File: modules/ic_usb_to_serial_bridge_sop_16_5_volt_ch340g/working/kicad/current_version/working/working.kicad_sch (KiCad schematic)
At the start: 5 parts, among them U1 isp16ch340g

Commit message: gitignore update mainly and update
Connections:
- net rx_atmega328 is gone; now on net rx_ch340: 111.1
- net tx_atmega328 is gone; now on net tx_ch340: 11.1
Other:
- note added: "ch340328_tx_rx_patch_block"
- note removed: "atmega328_tx_rx_patch_block"

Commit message: a few module workings
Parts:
- added R1, R2: r6o102, oomlout_oomp_part_footprints:r6o102_electronic_resistor_0603_1000_ohm, symbol oomlout_oomp_part_symbols:r6o102_electronic_resistor_0603_1000_ohm
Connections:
- net rx_ch340: now also R2.2; no longer U1.3 (RXD)
- net tx_ch340: now also R1.2; no longer U1.2 (TXD)
- new net: R2.1, U1.3 (RXD)
- new net: R1.1, U1.2 (TXD)
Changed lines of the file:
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@@
   (junction (at 134.62 107.95) (diameter 0) (color 0 0 0 0)
   )
+  (bus_entry (at 133.35 101.6) (size 2.54 2.54)
+    (stroke (width 0) (type default))
+  )
   (wire (pts (xy 123.19 114.3) (xy 134.62 114.3))
     (stroke (width 0) (type default))
@@
     (stroke (width 0) (type default))
   )
+  (wire (pts (xy 157.48 76.2) (xy 157.48 73.66))
+    (stroke (width 0) (type default))
+  )
   (wire (pts (xy 121.92 96.52) (xy 124.46 96.52))
     (stroke (width 0) (type default))
   )
+  (wire (pts (xy 154.94 76.2) (xy 157.48 76.2))
+    (stroke (width 0) (type default))
+  )
   (wire (pts (xy 134.62 114.3) (xy 134.62 116.84))
     (stroke (width 0) (type default))
@@
     (stroke (width 0) (type default))
   )
+  (wire (pts (xy 160.02 78.74) (xy 160.02 73.66))
+    (stroke (width 0) (type default))
+  )
   (wire (pts (xy 144.78 78.74) (xy 147.32 78.74))
     (stroke (width 0) (type default))
@@
   )
   (wire (pts (xy 125.73 140.97) (xy 129.54 140.97))
+    (stroke (width 0) (type default))
+  )
+  (wire (pts (xy 154.94 78.74) (xy 160.02 78.74))
     (stroke (width 0) (type default))
   )
@@
     (effects (font (size 1.27 1.27)) (justify right bottom))
   )
-  (label "rx_ch340" (at 147.32 78.74 0) (fields_autoplaced)
+  (label "rx_ch340" (at 160.02 73.66 90) (fields_autoplaced)
     (effects (font (size 1.27 1.27)) (justify left bottom))
   )
@@
     (effects (font (size 1.27 1.27)) (justify right bottom))
   )
-  (label "tx_ch340" (at 147.32 76.2 0) (fields_autoplaced)
+  (label "tx_ch340" (at 157.48 73.66 90) (fields_autoplaced)
     (effects (font (size 1.27 1.27)) (justify left bottom))
   )
@@
         (path "/c9993764-076f-44f6-bf4c-6b69ce17c9e4"
           (reference "11") (unit 1)
+        )
+      )
+    )
+  )
+  (symbol (lib_id "oomlout_oomp_part_symbols:r6o102_electronic_resistor_0603_1000_ohm") (at 151.13 78.74 90) (unit 1)
+    (in_bom yes) (on_board yes) (dnp no)
+    (property "Reference" "R2" (at 151.13 78.74 90)
+      (effects (font (size 1.27 1.27)))
+    )
+    (property "Value" "r6o102" (at 151.13 81.28 90)
+      (effects (font (size 1.27 1.27)) hide)
+    )
+    (property "Footprint" "oomlout_oomp_part_footprints:r6o102_electronic_resistor_0603_1000_ohm" (at 151.13 80.518 90)
+      (effects (font (size 1.27 1.27)) hide)
+    )
+    (property "Datasheet" "https://github.com/oomlout/oomlout_oomp_v3/parts/electronic_resistor_0603_1000_ohm/datasheet.pdf" (at 151.13 78.74 0)
+      (effects (font (size 1.27 1.27)) hide)
+    )
+    (pin "1")
+    (pin "2")
+    (instances
+      (project "working"
+        (path "/12ef09fc-ac25-49d7-9ff1-a1bc8f30d19c"
+          (reference "R2") (unit 1)
         )
       )
@@
         )
       )
+    )
+  )
+  (symbol (lib_id "oomlout_oomp_part_symbols:r6o102_electronic_resistor_0603_1000_ohm") (at 151.13 76.2 90) (unit 1)
+    (in_bom yes) (on_board yes) (dnp no)
+    (property "Reference" "R1" (at 151.13 76.2 90)
+      (effects (font (size 1.27 1.27)))
+    )
+    (property "Value" "r6o102" (at 151.13 73.66 90)
+      (effects (font (size 1.27 1.27)))
+    )
+    (property "Footprint" "oomlout_oomp_part_footprints:r6o102_electronic_resistor_0603_1000_ohm" (at 151.13 77.978 90)
+      (effects (font (size 1.27 1.27)) hide)
+    )
+    (property "Datasheet" "https://github.com/oomlout/oomlout_oomp_v3/parts/electronic_resistor_0603_1000_ohm/datasheet.pdf" (at 151.13 76.2 0)
+      (effects (font (size 1.27 1.27)) hide)
+    )
+    (pin "1")
+    (pin "2")
+    (instances
+      (project "working"
+        (path "/12ef09fc-ac25-49d7-9ff1-a1bc8f30d19c"
+          (reference "R1") (unit 1)
+        )
+      )

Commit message: a few module fixes
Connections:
- net xtal_1 renamed xtal1
- net xtal_2 renamed xtal2
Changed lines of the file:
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@@
     (effects (font (size 1.27 1.27)) (justify left bottom))
   )
-  (label "xtal_2" (at 121.92 96.52 180) (fields_autoplaced)
+  (label "xtal2" (at 121.92 96.52 180) (fields_autoplaced)
     (effects (font (size 1.27 1.27)) (justify right bottom))
   )
-  (label "xtal_1" (at 121.92 91.44 180) (fields_autoplaced)
+  (label "xtal1" (at 121.92 91.44 180) (fields_autoplaced)
     (effects (font (size 1.27 1.27)) (justify right bottom))
   )

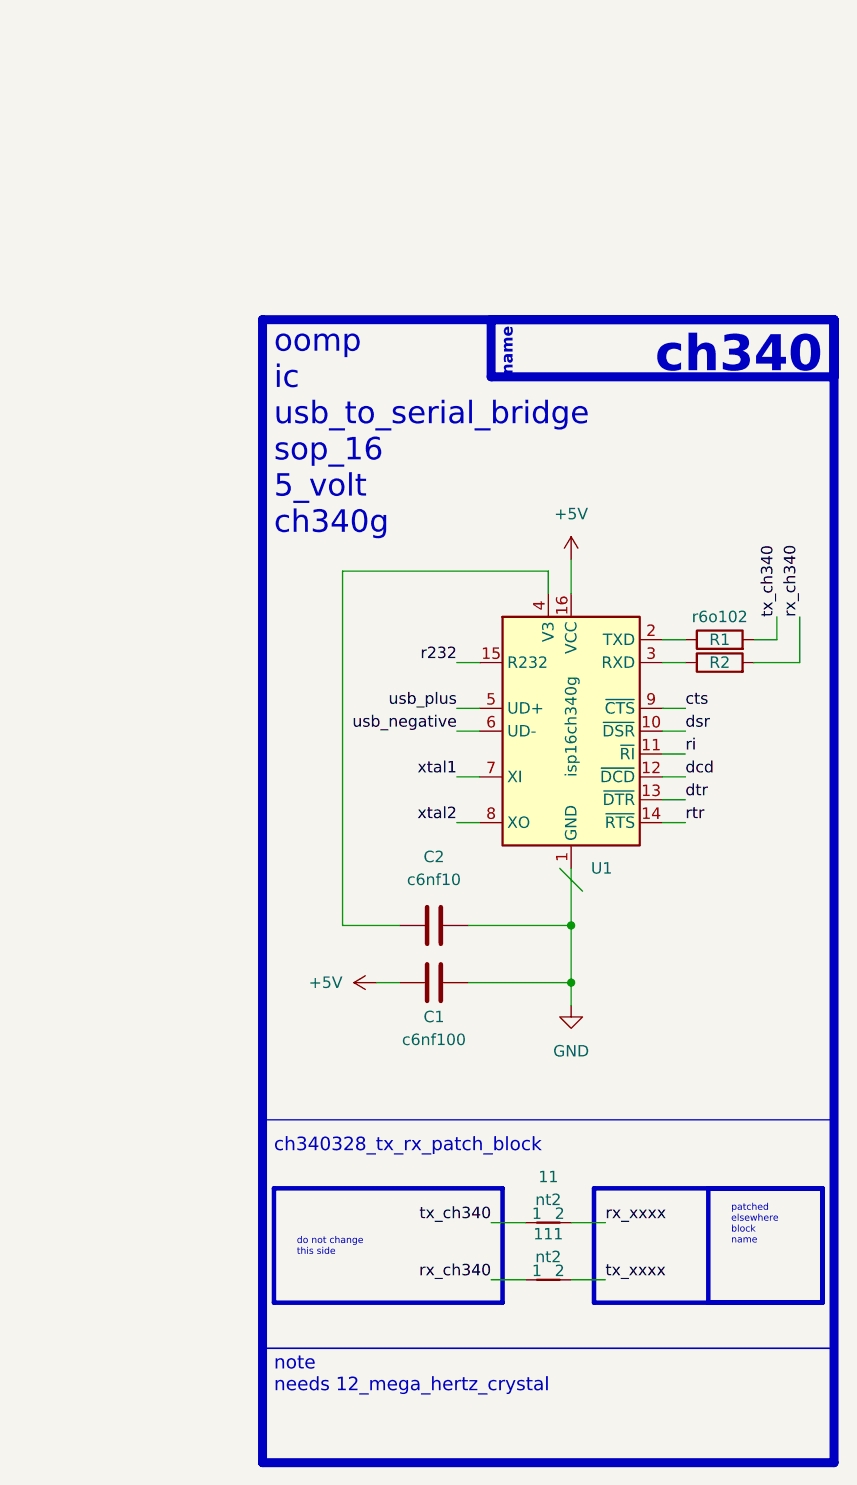
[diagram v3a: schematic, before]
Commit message: fixed formatting to be more consistent
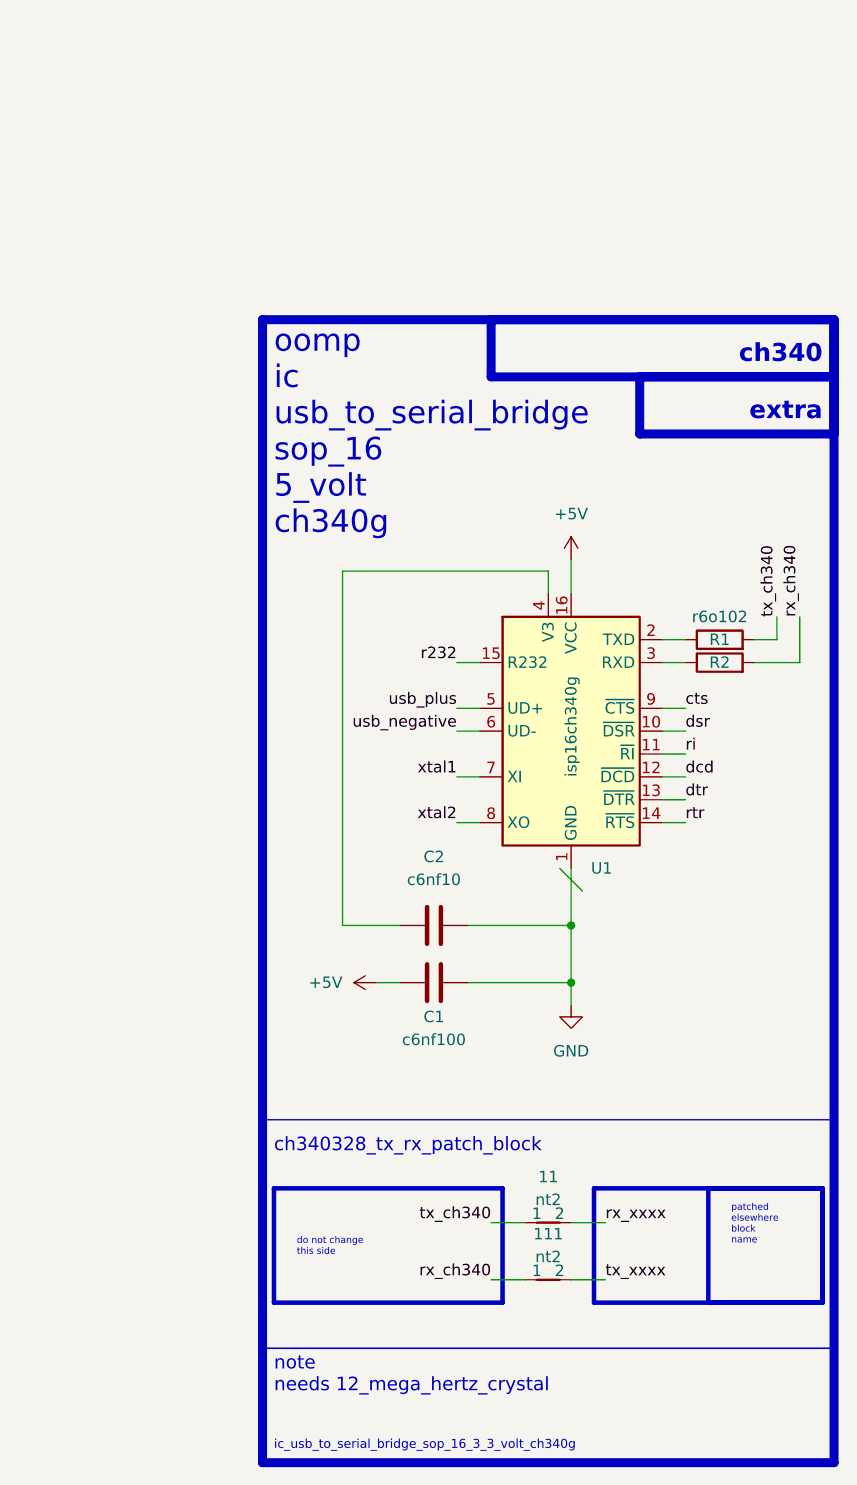
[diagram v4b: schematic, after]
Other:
- note added: "extra"
- note added: "ic_usb_to_serial_bridge_sop_16_3_3_volt_ch340g"
- note removed: "name"
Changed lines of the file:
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@@
   (rectangle (start 125.73 40.64) (end 163.83 46.99)
     (stroke (width 1) (type default))
-    (fill (type color) (color 0 0 0 0))
+    (fill (type none))
   )
   (rectangle (start 100.33 40.64) (end 163.83 167.64)
+    (stroke (width 1) (type default))
+    (fill (type none))
+  )
+  (rectangle (start 142.24 46.99) (end 163.83 53.34)
     (stroke (width 1) (type default))
     (fill (type none))
@@
     (effects (font (size 1.5 1.5)) (justify left bottom))
   )
-  (text "name" (at 128.27 46.99 90)
-    (effects (font (size 1.27 1.27) (thickness 0.254) bold (color 255 255 255 1)) (justify left bottom))
+  (text "extra" (at 162.56 52.07 0)
+    (effects (font (size 2 2) (thickness 0.8) bold) (justify right bottom))
   )
   (text "patched \nelsewhere\nblock \nname\n" (at 152.4 143.51 0)
@@
     (effects (font (size 0.75 0.75)) (justify left bottom))
   )
-  (text "ch340" (at 162.56 46.99 0)
-    (effects (font (size 4 4) (thickness 0.8) bold (color 255 255 255 1)) (justify right bottom))
+  (text "ch340" (at 162.56 45.72 0)
+    (effects (font (size 2 2) (thickness 0.8) bold) (justify right bottom))
+  )
+  (text "ic_usb_to_serial_bridge_sop_16_3_3_volt_ch340g" (at 101.6 166.37 0)
+    (effects (font (size 1 1)) (justify left bottom))
   )
   (text "oomp\nic\nusb_to_serial_bridge\nsop_16\n5_volt\nch340g" (at 101.6 64.77 0)

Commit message: schematic formatting
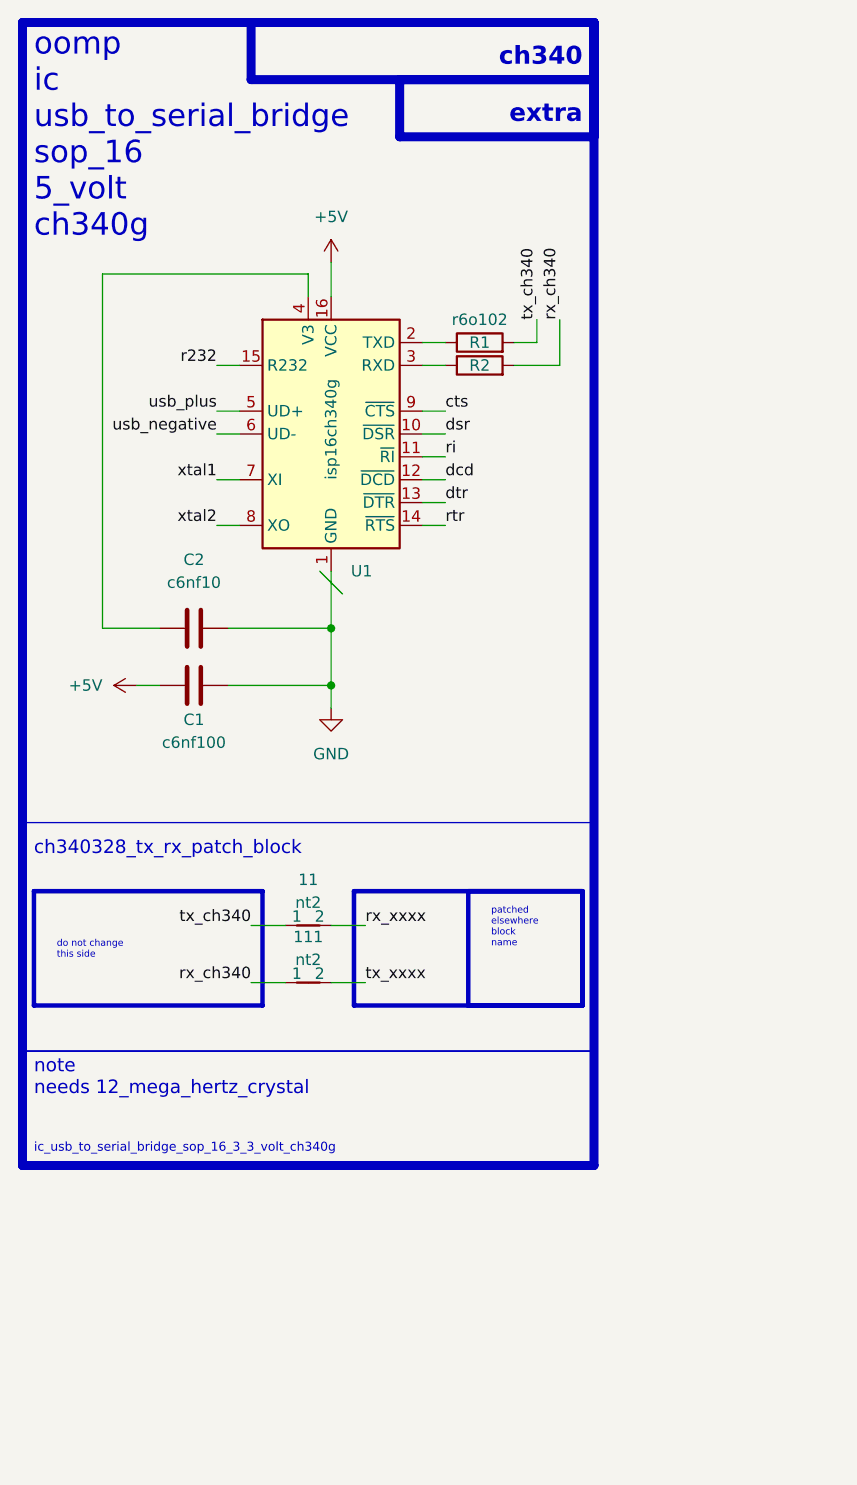
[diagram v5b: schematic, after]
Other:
- moved on the sheet: 11, 111, C1, C2, R1, R2, U1
